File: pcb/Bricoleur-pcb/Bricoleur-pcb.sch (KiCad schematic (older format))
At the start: 17 parts, among them U1 Ultrasonic-LV-EZ1, U2 PYNQ-Shield, U3 Ultrasonic-LV-EZ1, U4 Ultrasonic-LV-EZ1, U5 Arducam-OV5642, U6 Arducam-OV5642, U7 EFM32GG980

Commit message: Microcontroller power supply candidate
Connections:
- wire segments 104 -> 109
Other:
- note added: "STEMMER DETTE? USIKKER\n"
- moved on the sheet: R?
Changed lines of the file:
@@
 Text Label 950  3500 2    50   ~ 0
 PYNQ_5V0
-Wire Wire Line
-	9600 3900 8350 3900
 $Comp
 L Device:C C?
@@
 L Switch:SW_DPDT_x2 SW?
 U 1 1 5BC8006E
-P 9500 5400
-F 0 "SW?" H 9500 5685 50  0000 C CNN
-F 1 "SW_DPDT_x2" H 9500 5594 50  0000 C CNN
-F 2 "" H 9500 5400 50  0001 C CNN
-F 3 "" H 9500 5400 50  0001 C CNN
-	1    9500 5400
+P 9500 5500
+F 0 "SW?" H 9500 5785 50  0000 C CNN
+F 1 "SW_DPDT_x2" H 9500 5694 50  0000 C CNN
+F 2 "" H 9500 5500 50  0001 C CNN
+F 3 "" H 9500 5500 50  0001 C CNN
+	1    9500 5500
 	1    0    0    -1
 $EndComp
@@
 L Device:R R?
 U 1 1 5BC882E9
-P 8800 5400
-F 0 "R?" V 8593 5400 50  0000 C CNN
-F 1 "R" V 8684 5400 50  0000 C CNN
-F 2 "" V 8730 5400 50  0001 C CNN
-F 3 "~" H 8800 5400 50  0001 C CNN
-	1    8800 5400
+P 8800 5500
+F 0 "R?" V 8593 5500 50  0000 C CNN
+F 1 "R" V 8684 5500 50  0000 C CNN
+F 2 "" V 8730 5500 50  0001 C CNN
+F 3 "~" H 8800 5500 50  0001 C CNN
+	1    8800 5500
 	0    1    1    0
 $EndComp
 Wire Wire Line
-	8950 5400 9300 5400
+	8950 5500 9300 5500
+Wire Wire Line
+	9700 5400 9700 4950
+Wire Wire Line
+	9700 4950 9350 4950
+Text Label 9700 5600 0    50   ~ 0
+PYNQ_3V3
+Wire Wire Line
+	8350 3900 9350 3900
+Wire Wire Line
+	8650 5500 8350 5500
+Wire Wire Line
+	9350 3900 9350 4950
 Wire Bus Line
 	2750 650  2750 3700
@@
 Wire Bus Line
 	3000 6250 4850 6250
+Connection ~ 9350 3900
+Wire Wire Line
+	9350 3900 9600 3900
+Text Notes 8850 4900 0    50   ~ 10
+STEMMER DETTE? USIKKER\n
 $EndSCHEMATC

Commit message: Power supply done, debug interface started
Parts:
- removed R?: R, symbol Device:R
- added C? (x6): 100N, symbol Device:C
- added C? (x2): 10U, symbol Device:C
- added C? (x2): 10N, symbol Device:C
- added C?: 1uF, symbol Device:C
- added L?: L, symbol Device:L
- added R?: 1R, symbol Device:R
- added R?: 100R, symbol Device:R
- added SW?: SW_Push, symbol Switch:SW_Push
- gave numbers to parts that had none: 9
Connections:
- net labels added: AVDDU7, CAM_CLK, DEBUG_EXT_CABLE_ATTACH, VDDU7, VMCU, VSS07, VSSU7
- net labels removed: CamCLK
- wire segments 109 -> 143
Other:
- note added: "POWER SUPPLY\n - Bør dobbeltsjekkes \n"
- note removed: "STEMMER DETTE? USIKKER\n"

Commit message: Schematics and footprints almost done
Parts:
- removed SW1: SW_DPDT_x2, symbol Switch:SW_DPDT_x2
- added U11: SW_DP3T, Bricoleur-custom:SW_CK_JS203011, symbol Bricoleur-pcb-cache:SW_DP3T
- C1: value C -> 1U; footprint (none) -> Capacitor_SMD:C_0201_0603Metric
- C10, C11, C12, C3, C6, C7, C8, C9: renamed from C?; footprint (none) -> Capacitor_SMD:C_0402_1005Metric
- C13, C5: renamed from C?; footprint (none) -> Capacitor_SMD:C_0805_2012Metric
- C2: value C -> 4U7; footprint (none) -> Capacitor_SMD:C_0805_2012Metric
- C4: renamed from C?; footprint (none) -> Capacitor_SMD:C_0603_1608Metric
- L1: value L -> 220R 2A CBF221HC; footprint (none) -> Bricoleur-custom:CBF221HC
- L2: renamed from L?; value L -> CBF102WB; footprint (none) -> Bricoleur-custom:CBF102WB
- R1, R4: renamed from R?; footprint (none) -> Resistor_SMD:R_0402_1005Metric
- R2, R3: value R -> 15R; footprint (none) -> Resistor_SMD:R_0402_1005Metric
- SW2: renamed from SW?; footprint (none) -> Bricoleur-custom:SWITCH_WURTH_4301182043816
- U1, U3, U4: value Ultrasonic-LV-EZ1 -> Ultrasonic-LV-EZ0; footprint (none) -> Connector_PinHeader_2.54mm:PinHeader_1x07_P2.54mm_Vertical; symbol Bricoleur-pcb-cache:Ultrasonic-LV-EZ1 -> Bricoleur-pcb-cache:Bricoleur-pcb-cache_Ultrasonic-LV-EZ0
- U5, U6: footprint (none) -> Connector_PinHeader_2.54mm:PinHeader_1x20_P2.54mm_Vertical
- U9: footprint SOT95P275X110-6N -> (none)
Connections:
- net labels added: DBG_LED_1, DBG_LED_2, DBG_LED_3, DBG_PB_1, DBG_PB_2, DBG_PB_3, DBG_Supply, DH_TCK_SWCLK, DH_TDO_SWO, DH_TMS_SWDIO
- wire segments 143 -> 153
- no-connect marks 0 -> 1
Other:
- note removed: "Not finished!\n"

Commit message: Start of layout work + minor tweaks
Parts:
- removed U2: PYNQ-Shield, symbol Bricoleur-pcb-cache:PYNQ-Shield
- added J3: Conn_01x04_Male, symbol Connector:Conn_01x04_Male
- added TP1: Test_VMCU, symbol Connector:TestPoint
- added U2: PYNQ-Shield-Bricoleur-pcb-cache, Bricoleur-custom:PYNQ_Shield, symbol Bricoleur-pcb-cache:PYNQ-Shield-Bricoleur-pcb-cache
- J1: footprint (none) -> Connector_USB:USB_B_OST_USB-B1HSxx_Horizontal
- U1, U3, U4: footprint Connector_PinHeader_2.54mm:PinHeader_1x07_P2.54mm_Vertical -> Connector_IDC:IDC-Header_2x03_P2.54mm_Vertical
- U5, U6: footprint Connector_PinHeader_2.54mm:PinHeader_1x20_P2.54mm_Vertical -> Connector_IDC:IDC-Header_2x10_P2.54mm_Vertical
- U8: footprint (none) -> Connector_PinHeader_2.54mm:PinHeader_1x03_P2.54mm_Vertical
- U9: footprint (none) -> Bricoleur-custom:IP4220CZ6
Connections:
- net labels added: CAM0_PCLK, DH_#RESET
- net labels removed: CAM0_XCLK
- wire segments 153 -> 174
- no-connect marks 1 -> 83
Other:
- moved on the sheet: C3, R1, SW2

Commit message: Finished camera connection, started on MC. Changed debug protection diodes sharing pattern to match debug connector.
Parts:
- U1, U3, U4: symbol Bricoleur-pcb-cache:Bricoleur-pcb-cache_Ultrasonic-LV-EZ0 -> Bricoleur-pcb-rescue:Bricoleur-pcb-cache_Ultrasonic-LV-EZ0-Bricoleur-pcb-cache
- U11: symbol Bricoleur-pcb-cache:SW_DP3T -> Bricoleur-pcb-rescue:SW_DP3T-Bricoleur-pcb-cache
- U2: symbol Bricoleur-pcb-cache:PYNQ-Shield-Bricoleur-pcb-cache -> Bricoleur-pcb-rescue:PYNQ-Shield-Bricoleur-pcb-cache-Bricoleur-pcb-cache
- U5, U6: symbol Bricoleur-pcb-cache:Arducam-OV5642 -> Bricoleur-pcb-rescue:Arducam-OV5642-Bricoleur-pcb-cache
- U7: symbol symbols:EFM32GG980 -> Bricoleur-pcb-rescue:EFM32GG980-symbols
- U8: symbol Bricoleur-pcb-cache:UART_BOOT -> Bricoleur-pcb-rescue:UART_BOOT-Bricoleur-pcb-cache
- U9: symbol IP4220CZ6:IP4220CZ6 -> Bricoleur-pcb-rescue:IP4220CZ6-IP4220CZ6
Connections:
- net labels added: PULSE
- wire segments 174 -> 161
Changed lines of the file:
@@
 $EndDescr
 $Comp
-L Bricoleur-pcb-cache:Arducam-OV5642 U5
+L Bricoleur-pcb-rescue:Arducam-OV5642-Bricoleur-pcb-cache U5
 U 1 1 5B998412
 P 4200 5200
@@
 $EndComp
 $Comp
-L Bricoleur-pcb-cache:Arducam-OV5642 U6
+L Bricoleur-pcb-rescue:Arducam-OV5642-Bricoleur-pcb-cache U6
 U 1 1 5B99848C
 P 4200 7450
@@
 GND
 $Comp
-L symbols:EFM32GG980 U7
+L Bricoleur-pcb-rescue:EFM32GG980-symbols U7
 U 1 1 5B9A6C8F
 P 6150 1200
@@
 $EndComp
 $Comp
-L Bricoleur-pcb-cache:Bricoleur-pcb-cache_Ultrasonic-LV-EZ0 U1
+L Bricoleur-pcb-rescue:Bricoleur-pcb-cache_Ultrasonic-LV-EZ0-Bricoleur-pcb-cache U1
 U 1 1 5B9AE131
 P 4150 1450
@@
 $EndComp
 $Comp
-L Bricoleur-pcb-cache:Bricoleur-pcb-cache_Ultrasonic-LV-EZ0 U3
+L Bricoleur-pcb-rescue:Bricoleur-pcb-cache_Ultrasonic-LV-EZ0-Bricoleur-pcb-cache U3
 U 1 1 5B9AE194
 P 5450 2300
@@
 $EndComp
 $Comp
-L Bricoleur-pcb-cache:Bricoleur-pcb-cache_Ultrasonic-LV-EZ0 U4
+L Bricoleur-pcb-rescue:Bricoleur-pcb-cache_Ultrasonic-LV-EZ0-Bricoleur-pcb-cache U4
 U 1 1 5B9AE2C4
 P 4100 2600
@@
 	9400 3050 9400 3700
 $Comp
-L IP4220CZ6:IP4220CZ6 U9
+L Bricoleur-pcb-rescue:IP4220CZ6-IP4220CZ6 U9
 U 1 1 5BA09E46
 P 10450 2300
@@
 GND
 $Comp
-L Bricoleur-pcb-cache:UART_BOOT U8
+L Bricoleur-pcb-rescue:UART_BOOT-Bricoleur-pcb-cache U8
 U 1 1 5BA26E40
 P 8800 1100
@@
 Entry Wire Line
 	2800 5500 2900 5600
-Wire Wire Line
-	2700 7350 2250 7350
-Wire Wire Line
-	2700 7450 2250 7450
-Wire Wire Line
-	2700 7550 2250 7550
-Wire Wire Line
-	2700 7650 2250 7650
-Wire Wire Line
-	2700 7750 2250 7750
-Wire Wire Line
-	2700 7850 2250 7850
-Wire Wire Line
-	2700 7950 2250 7950
-Wire Wire Line
-	2700 8050 2250 8050
-Wire Wire Line
-	2700 8150 2250 8150
 Text Label 3650 6950 1    50   ~ 0
 CAM0_DOUT2
@@
 Text Label 2350 5100 0    50   ~ 0
 CAM0_HREF
-Wire Wire Line
-	2700 8250 2250 8250
 Entry Wire Line
 	2800 5400 2900 5500
 Entry Wire Line
 	2800 5300 2900 5400
-Wire Wire Line
-	2700 7250 2250 7250
-Wire Wire Line
-	2700 7150 2250 7150
-Wire Wire Line
-	2700 7050 2250 7050
 Text Label 2350 5900 0    50   ~ 0
 CAM0_VSYNC
@@
 $EndSheet
 $Comp
-L Bricoleur-pcb-cache:SW_DP3T U11
+L Bricoleur-pcb-rescue:SW_DP3T-Bricoleur-pcb-cache U11
 U 1 1 5BAC4FA8
 P 10450 5200
@@
 NoConn ~ 6150 1400
 $Comp
-L Bricoleur-pcb-cache:PYNQ-Shield-Bricoleur-pcb-cache U2
+L Bricoleur-pcb-rescue:PYNQ-Shield-Bricoleur-pcb-cache-Bricoleur-pcb-cache U2
 U 1 1 5BADF788
 P 1650 2600
@@
 Wire Bus Line
 	2900 3600 2900 4850
+Text GLabel 5900 1200 1    50   Input ~ 0
+PULSE
 $EndSCHEMATC

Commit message: More ESD protection, USART output, more footprints
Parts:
- removed J3: Conn_01x04_Male, symbol Connector:Conn_01x04_Male
- removed U1, U3, U4: Ultrasonic-LV-EZ0, Connector_IDC:IDC-Header_2x03_P2.54mm_Vertical, symbol Bricoleur-pcb-rescue:Bricoleur-pcb-cache_Ultrasonic-LV-EZ0-Bricoleur-pcb-cache
- J1: footprint Connector_USB:USB_B_OST_USB-B1HSxx_Horizontal -> Connector_USB:USB_Micro-B_Amphenol_10103594-0001LF_Horizontal
- TP1: footprint (none) -> Connector_PinSocket_2.54mm:PinSocket_1x02_P2.54mm_Vertical; symbol Connector:TestPoint -> Connector:TestPoint_2Pole
- U8: footprint Connector_PinHeader_2.54mm:PinHeader_1x03_P2.54mm_Vertical -> Connector_IDC:IDC-Header_2x03_P2.54mm_Vertical; symbol Bricoleur-pcb-rescue:UART_BOOT-Bricoleur-pcb-cache -> Connector_Generic:Conn_02x03_Odd_Even
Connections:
- net labels added: US1_CLK, US1_RX, US1_TX
- net labels removed: DBG_Supply, US0_CS
- wire segments 161 -> 156
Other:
- moved on the sheet: J1, R2, R3, U9

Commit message: PCB…
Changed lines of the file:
@@
 $EndComp
-Wire Wire Line
-	9300 1750 9300 2750
 Wire Wire Line
 	10700 1850 9400 1850
@@
 	-1   0    0    1
 $EndComp
-Wire Wire Line
-	9750 2750 9300 2750
-Connection ~ 9300 2750
 Text Label 11150 2550 1    50   ~ 0
 GND
 Wire Wire Line
 	11150 2750 11150 3000
-Wire Wire Line
-	11150 3000 9600 3000
-Connection ~ 9600 3000
 Wire Wire Line
 	9600 3000 9600 2050
@@
 $EndSheet
 Wire Wire Line
-	9300 2750 9300 3350
-Wire Wire Line
 	10700 2050 9600 2050
 $Sheet
@@
 F4 "TX" I R 2450 1700 50
 $EndSheet
-Entry Wire Line
-	5600 1650 5700 1750
 Entry Wire Line
 	2900 1400 3000 1500
@@
 Wire Wire Line
 	8350 1800 8750 1800
+Connection ~ 8750 1550
+Wire Bus Line
+	2900 3600 2900 4850
+Wire Bus Line
+	3000 6250 4850 6250
+Wire Bus Line
+	2900 5100 2900 6550
+Wire Bus Line
+	2900 6550 4850 6550
+Wire Bus Line
+	3000 650  3000 4750
+Wire Bus Line
+	3050 4750 3050 5650
+Wire Bus Line
+	8950 2700 8950 4200
+Wire Wire Line
+	2350 5200 2950 5200
+Wire Wire Line
+	8350 4000 9050 4000
 Wire Wire Line
 	2350 5700 2950 5700
 Wire Wire Line
-	8350 4000 9050 4000
-Wire Wire Line
-	2350 5200 2950 5200
-Wire Bus Line
-	8950 2700 8950 4200
-Wire Bus Line
-	3050 4750 3050 5650
-Wire Bus Line
-	3000 650  3000 4750
-Wire Bus Line
-	2900 6550 4850 6550
-Wire Bus Line
-	2900 5100 2900 6550
-Wire Bus Line
-	3000 6250 4850 6250
-Wire Bus Line
-	2900 3600 2900 4850
-Connection ~ 8750 1550
+	11150 3000 9600 3000
+Connection ~ 9600 3000
+Wire Wire Line
+	9300 2750 9300 3350
+Wire Wire Line
+	9300 1750 9300 2750
+Connection ~ 9300 2750
+Wire Wire Line
+	9750 2750 9300 2750
 $EndSCHEMATC

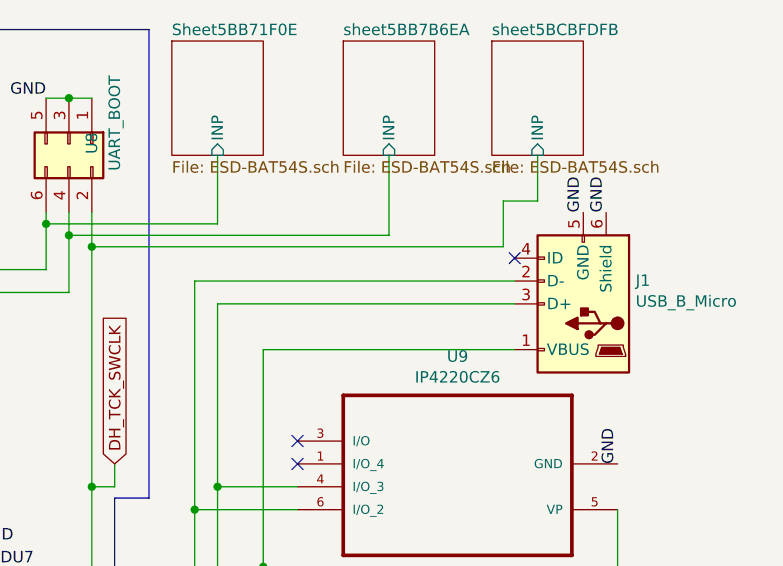
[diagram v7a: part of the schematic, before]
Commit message: Narrowed down component placement, continued routing
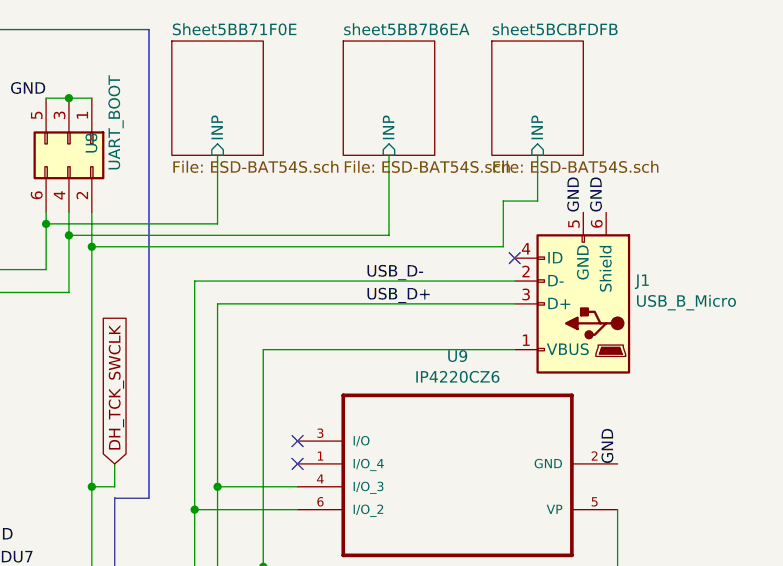
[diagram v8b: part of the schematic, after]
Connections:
- net USB_D-: now reaches J1.2 (D-), R2.2, U9.6 (I/O_2)
- net USB_D+: now reaches J1.3 (D+), R3.1, U9.4 (I/O_3)
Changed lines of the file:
@@
 	8350 1800 8750 1800
 Connection ~ 8750 1550
-Wire Bus Line
-	2900 3600 2900 4850
-Wire Bus Line
-	3000 6250 4850 6250
-Wire Bus Line
-	2900 5100 2900 6550
-Wire Bus Line
-	2900 6550 4850 6550
-Wire Bus Line
-	3000 650  3000 4750
-Wire Bus Line
-	3050 4750 3050 5650
-Wire Bus Line
-	8950 2700 8950 4200
-Wire Wire Line
-	2350 5200 2950 5200
-Wire Wire Line
-	8350 4000 9050 4000
-Wire Wire Line
-	2350 5700 2950 5700
 Wire Wire Line
 	11150 3000 9600 3000
@@
 Wire Wire Line
 	9750 2750 9300 2750
+Wire Wire Line
+	2350 5200 2950 5200
+Wire Wire Line
+	8350 4000 9050 4000
+Wire Wire Line
+	2350 5700 2950 5700
+Wire Bus Line
+	8950 2700 8950 4200
+Wire Bus Line
+	3000 650  3000 4750
+Wire Bus Line
+	3050 4750 3050 5650
+Wire Bus Line
+	2900 6550 4850 6550
+Wire Bus Line
+	2900 5100 2900 6550
+Wire Bus Line
+	3000 6250 4850 6250
+Wire Bus Line
+	2900 3600 2900 4850
+Text Label 10050 1750 0    50   ~ 0
+USB_D-
+Text Label 10050 1850 0    50   ~ 0
+USB_D+
 $EndSCHEMATC
